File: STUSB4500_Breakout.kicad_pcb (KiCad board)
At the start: 4 copper layers, 25.4 x 25.4 mm, 32 parts, among them J1 USB_C_Receptacle, J2 STEMMA_I2C_QT, J3 STEMMA_I2C_QT, J4 Screw_Terminal_01x02, Q1 STL6P3LLH6, U1 STUSB4500QTR

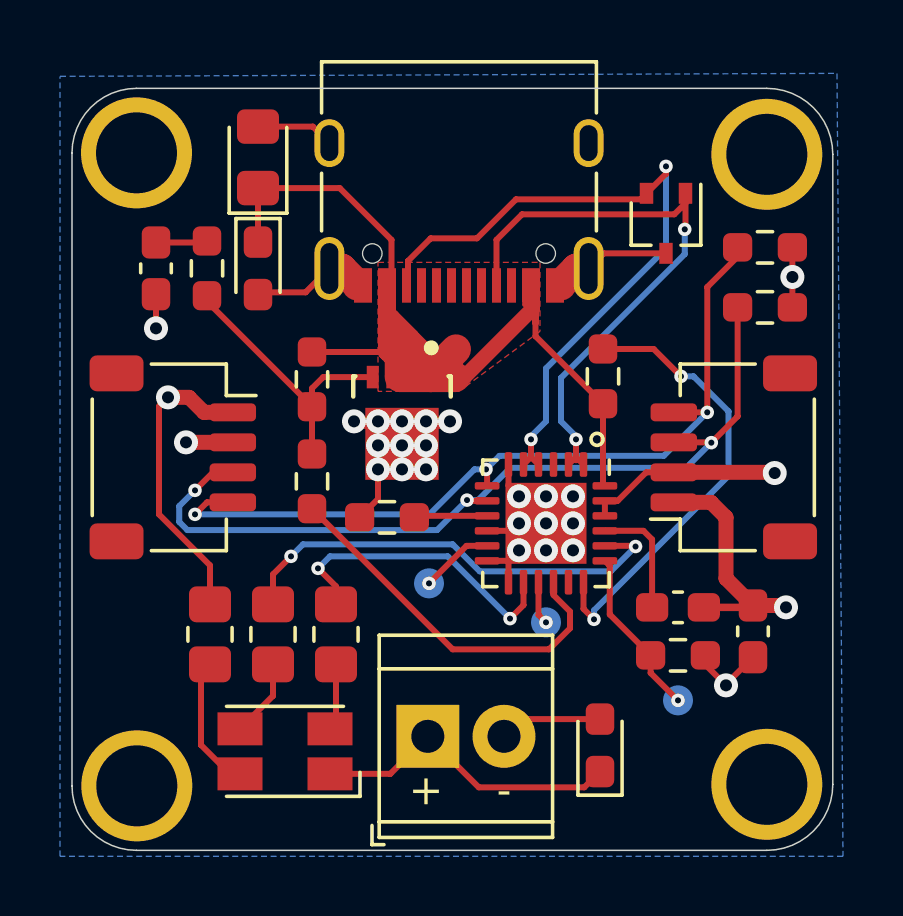
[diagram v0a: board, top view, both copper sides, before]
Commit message: Updated routing as suggested my Mark Olsson @k0d
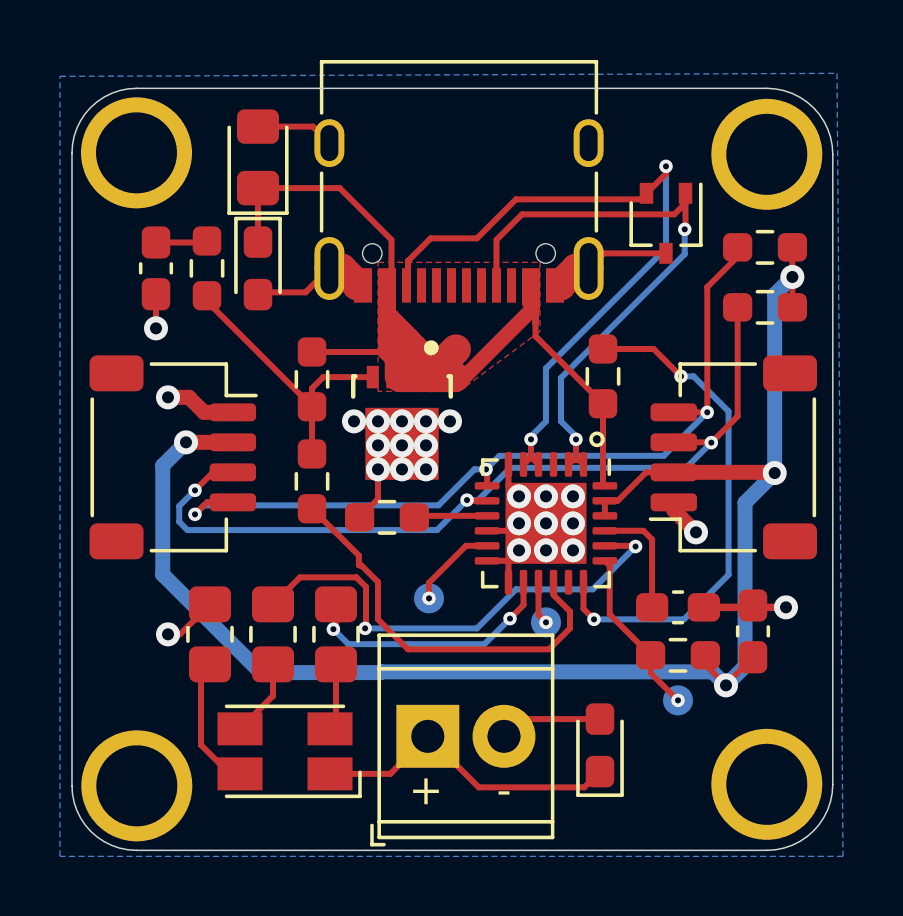
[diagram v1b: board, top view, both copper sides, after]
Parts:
- moved ATTACH 0.50 mm to (120.7, 53.5)
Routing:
- net VCC: track 12.7 -> 52.3 mm
- net GND: track 42.2 -> 31.3 mm, vias 11 -> 13
- net Net-(R8-Pad1): track 15.2 -> 17.0 mm
- net PDO3: track 10.3 -> 8.71 mm
- net PDO2: track 15.2 -> 16.2 mm
- net VBUS_EN_SNK: track 12.6 -> 13.5 mm
- net ATTACH: track 2.46 -> 2.97 mm
- added copper zone on B.Cu, net GND
- removed copper zone on B.Cu, net VCC

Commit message: Updated ready for manufacturing
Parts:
- added G***: LOGO, Makeristic-KiCad-Library:stemma_qt_logo, B.Cu at (132.5, 48.8)
- added G***: LOGO, Makeristic-KiCad-Library:stemma_qt_logo, B.Cu at (110.5, 49.0)
- moved GPIO 0.58 mm to (124.9, 54.8)
- moved D4 0.22 mm to (126.2, 58.5)
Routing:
- net VBUS_EN_SNK: track 13.5 -> 14.7 mm
- net GPIO: track 1.44 -> 2.07 mm
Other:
- board text added: "STUSB4500 Breakout makeristic.com"
- board text removed: "STUSB4500 Breakout makeristic.io"
